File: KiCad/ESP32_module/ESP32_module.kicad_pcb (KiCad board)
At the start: 2 copper layers, 40 x 40 mm, 39 parts, among them J1 Conn_01x05_Pin, J2 Conn_01x05_Pin, J3 Conn_01x05_Pin, J4 Conn_01x05_Pin, J5 Conn_01x02_Pin, J6 Conn_01x02_Pin, J7 Conn_01x02_Pin, J8 Conn_01x02_Pin, J9 Conn_01x02_Pin, M1 ESP32_XAIO

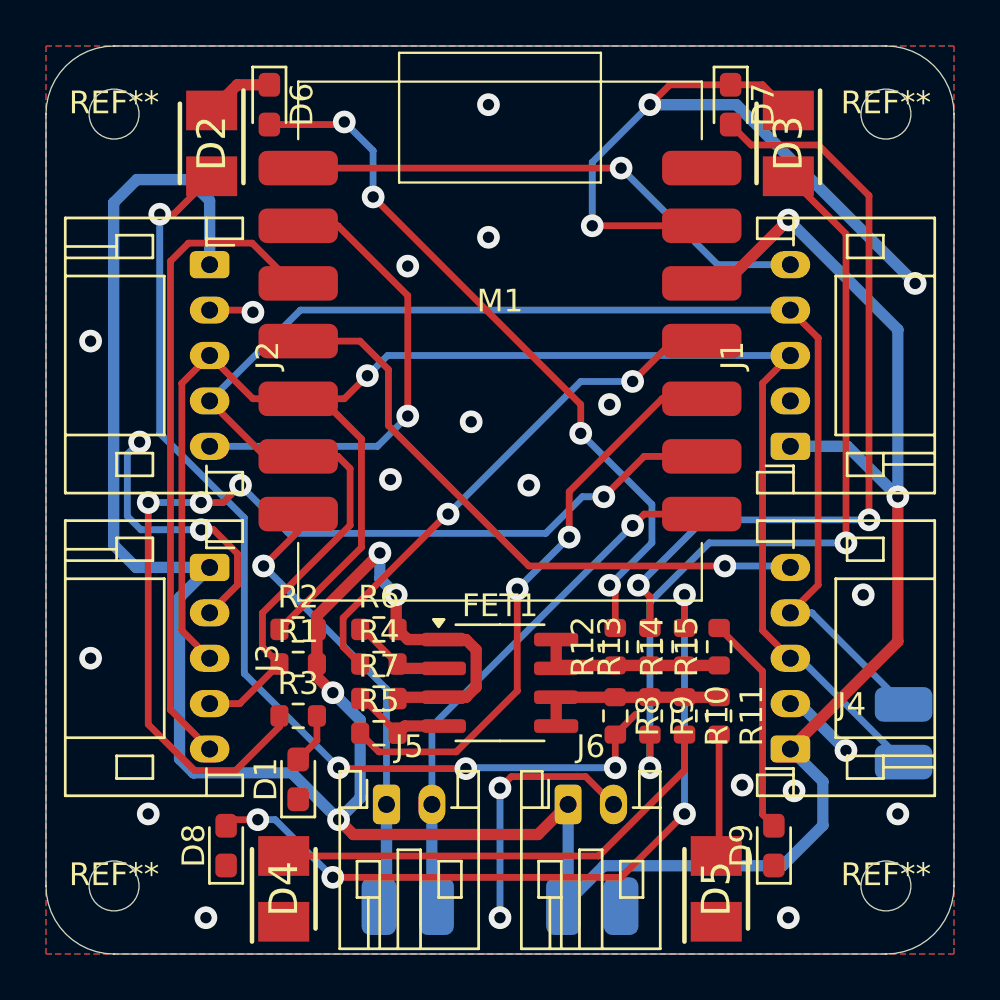
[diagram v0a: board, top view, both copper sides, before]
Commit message: Complite ESP32_module PCB design
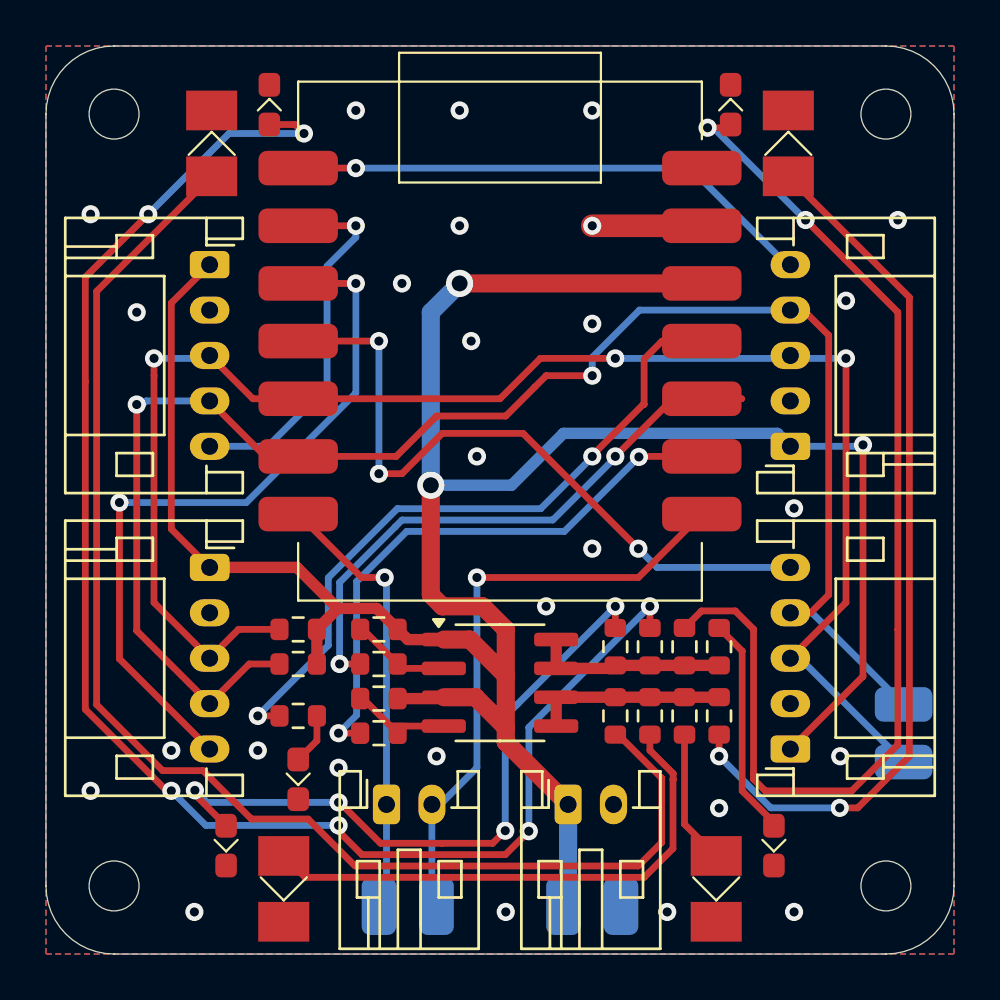
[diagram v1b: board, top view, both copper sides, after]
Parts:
- moved R14 3.05 mm to (182.9, 102.4)
- moved R9 3.05 mm to (187.5, 105.4)
- moved R10 1.52 mm to (184.4, 105.4)
- moved R11 1.52 mm to (185.9, 105.4)
- moved R12 1.52 mm to (184.4, 102.4)
- moved R13 1.52 mm to (185.9, 102.4)
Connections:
- R3 pad 1: Net-(M1-D8) -> Net-(M1-D10)
- R4 pad 1: Net-(M1-D10) -> Net-(M1-D9)
- R5 pad 1: Net-(M1-D9) -> Net-(M1-D8)
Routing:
- net GND1: track 64.9 -> 4.83 mm, vias 25 -> 27
- net Net-(D6-A): track 32.1 -> 68.8 mm, vias 4 -> 6
- net +3.3V: track 141.8 -> 115.1 mm, vias 6 -> 3
- net Net-(M1-D8): track 44.7 -> 25.5 mm, vias 4 -> 2
- net Net-(D7-A): track 35.1 -> 49.6 mm
- net Net-(D2-A): track 45.6 -> 59.3 mm, vias 4 -> 0
- net Net-(M1-D10): track 23.2 -> 30.3 mm
- net SDA: track 76.1 -> 71.1 mm, vias 1 -> 3
- net /XSHOUT_B: track 20.7 -> 16.4 mm
- net Net-(D8-A): track 33.6 -> 29.8 mm
- net SCL: track 70.0 -> 73.6 mm, vias 0 -> 2
- net /XSHOUT_D: track 27.3 -> 30.7 mm, vias 1 -> 3
- net /XSHOUT_C: track 28.9 -> 32.3 mm, vias 0 -> 2
- net Net-(D3-A): track 35.7 -> 39.0 mm
- net RX: track 23.8 -> 26.7 mm
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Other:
- board text added: "3.3V"
- board text added: "GND"
- board text added: "PORT-A"
- board text added: "PORT-B"
- board text added: "PORT-C"
- board text added: "PORT-D"
- board text added: "RX"
- board text added: "SCL"
- board text added: "SDA"
- board text added: "TX"
